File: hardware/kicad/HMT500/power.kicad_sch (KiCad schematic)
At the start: 22 parts, among them U1 TPS26600, U2 LMR36006, U3 TPS7A2033PDBVR

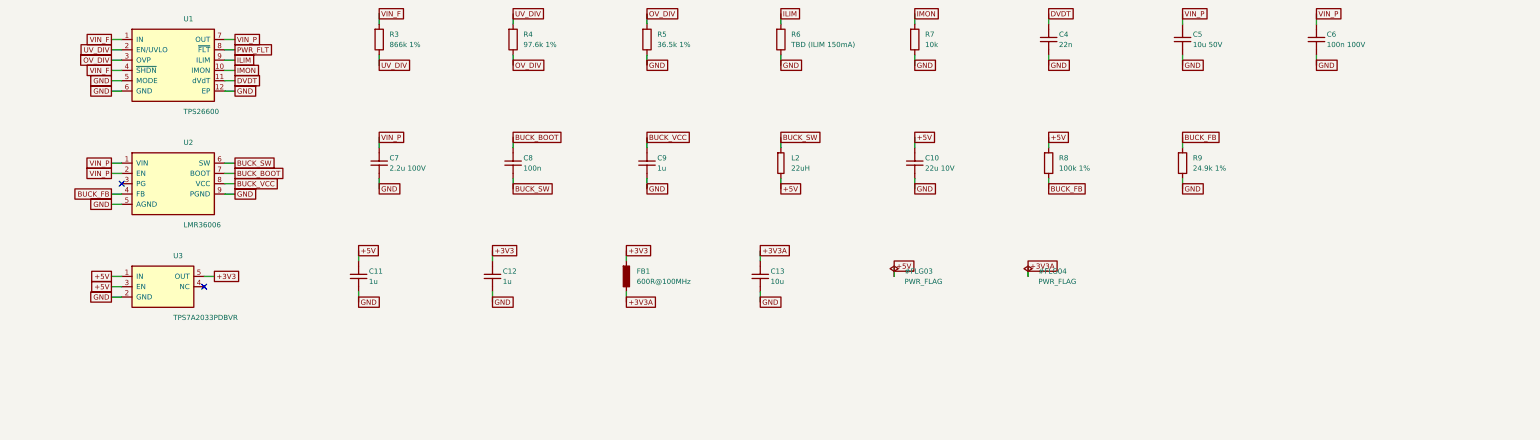
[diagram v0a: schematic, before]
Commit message: KiCad schematic v0.2: hand-laid-out, wired, readable sheets with power symbols and functional blocks
Replaces the label-only v0.1. Drawing rules are validated at generation and
the drawn netlist is checked against design intent (71 nets, 0 errors).

Co-Authored-By: Claude Opus 5.5 <noreply@anthropic.com>
Claude-Session: https://claude.ai/code/session_01JA2o8uJsqp9Vzsg4b665ev
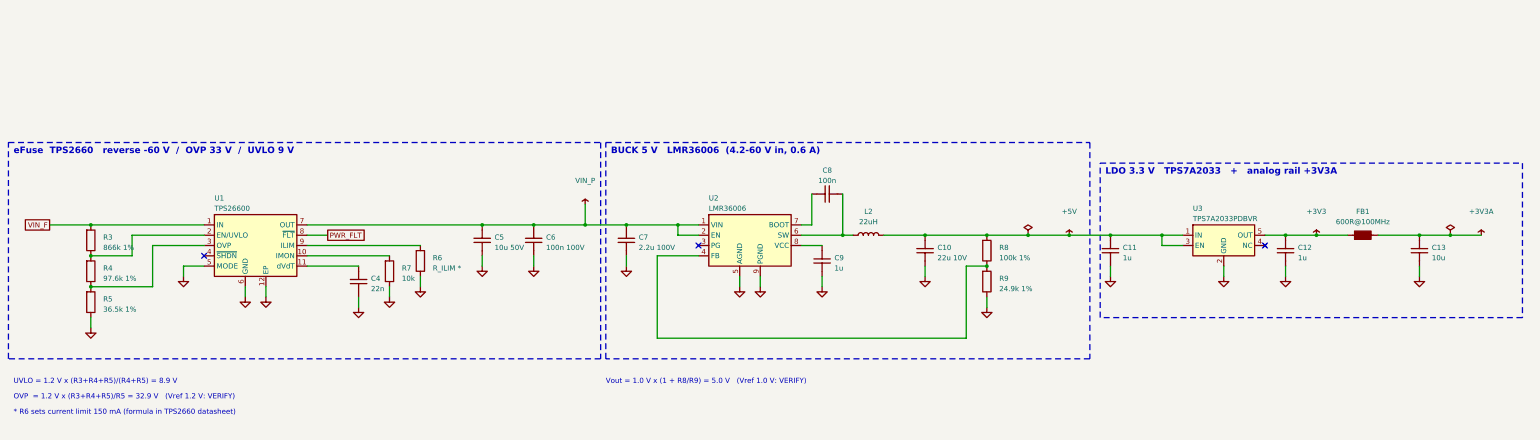
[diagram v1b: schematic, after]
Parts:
- C5, C7: footprint Capacitor_SMD:C_1206_3216Metric -> Capacitor_SMD:C_1210_3225Metric
- R6: value TBD (ILIM 150mA) -> R_ILIM *
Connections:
- net VIN_F: no longer U1.4 (~{SHDN})
- net BUCK_BOOT: no longer names the net of C8.1, U2.7 (BOOT)
- net BUCK_FB: no longer names the net of R8.2, R9.1, U2.4 (FB)
- net BUCK_SW: no longer names the net of C8.2, L2.1, U2.6 (SW)
- net BUCK_VCC: no longer names the net of C9.1, U2.8 (VCC)
- net DVDT: no longer names the net of C4.1, U1.11 (dVdT)
- net ILIM: no longer names the net of R6.1, U1.9 (ILIM)
- net IMON: no longer names the net of R7.1, U1.10 (IMON)
- net OV_DIV: no longer names the net of R4.2, R5.1, U1.3 (OVP)
- net UV_DIV: no longer names the net of R3.2, R4.1, U1.2 (EN/UVLO)
- no-connect marks 2 -> 3
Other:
- note added: "* R6 sets current limit 150 mA (formula in TPS2660 datasheet)"
- note added: "BUCK 5 V LMR36006 (4.2-60 V in, 0.6 A)"
- note added: "LDO 3.3 V TPS7A2033 + analog rail +3V3A"
- note added: "OVP = 1.2 V x (R3+R4+R5)/R5 = 32.9 V (Vref 1.2 V: VERIFY)"
- note added: "UVLO = 1.2 V x (R3+R4+R5)/(R4+R5) = 8.9 V"
- note added: "Vout = 1.0 V x (1 + R8/R9) = 5.0 V (Vref 1.0 V: VERIFY)"
- note added: "eFuse TPS2660 reverse -60 V / OVP 33 V / UVLO 9 V"
- title: HMT500 - eFuse, buck 5V, LDO 3.3V -> HMT500  Power
- moved on the sheet: C10, C11, C12, C13, C4, C5, C6, C7, C8, C9, R3, R4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

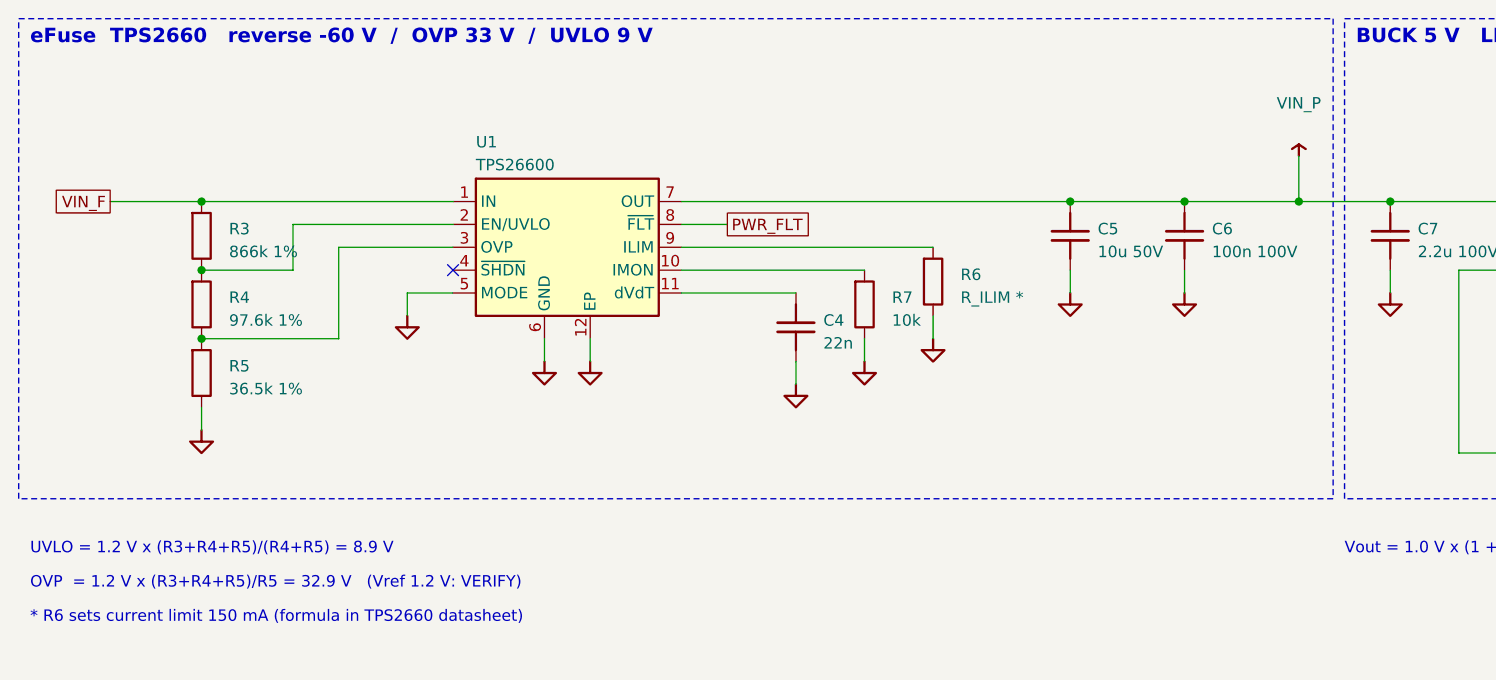
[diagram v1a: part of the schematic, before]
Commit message: Schematic v0.3, purchase parts list, studio product renders
- Schematic v0.3: TPS26600PWPR now uses the official KiCad pinout
  (HTSSOP-16: dual IN/OUT, UVLO, OVP, SHDN, MODE, RTN, EP). RTN is
  split onto its own net EF_RTN with a 0R link R22, flagged for
  datasheet confirmation, because tying RTN to GND disables the
  reverse-polarity protection. The ADS1220 pinout matches the official
  symbol. Netlist check passes: 70 nets, 0 errors. Rev bumped and cover
  notes updated.
- make_parts_list.py: purchase parts list (xlsx + csv) built from the
  KiCad BOM. It adds manufacturer, MPN, 1k price estimates and status,
  plus a per-category summary sheet with an FX input.
- render_studio.py: studio-style product renders (PBR stainless,
  image-based lighting, SSAO, contact shadow, laser marking, thread and
  connector pin detail). Six shots, including a cutaway.

Co-Authored-By: Claude Opus 5.5 <noreply@anthropic.com>
Claude-Session: https://claude.ai/code/session_01JA2o8uJsqp9Vzsg4b665ev
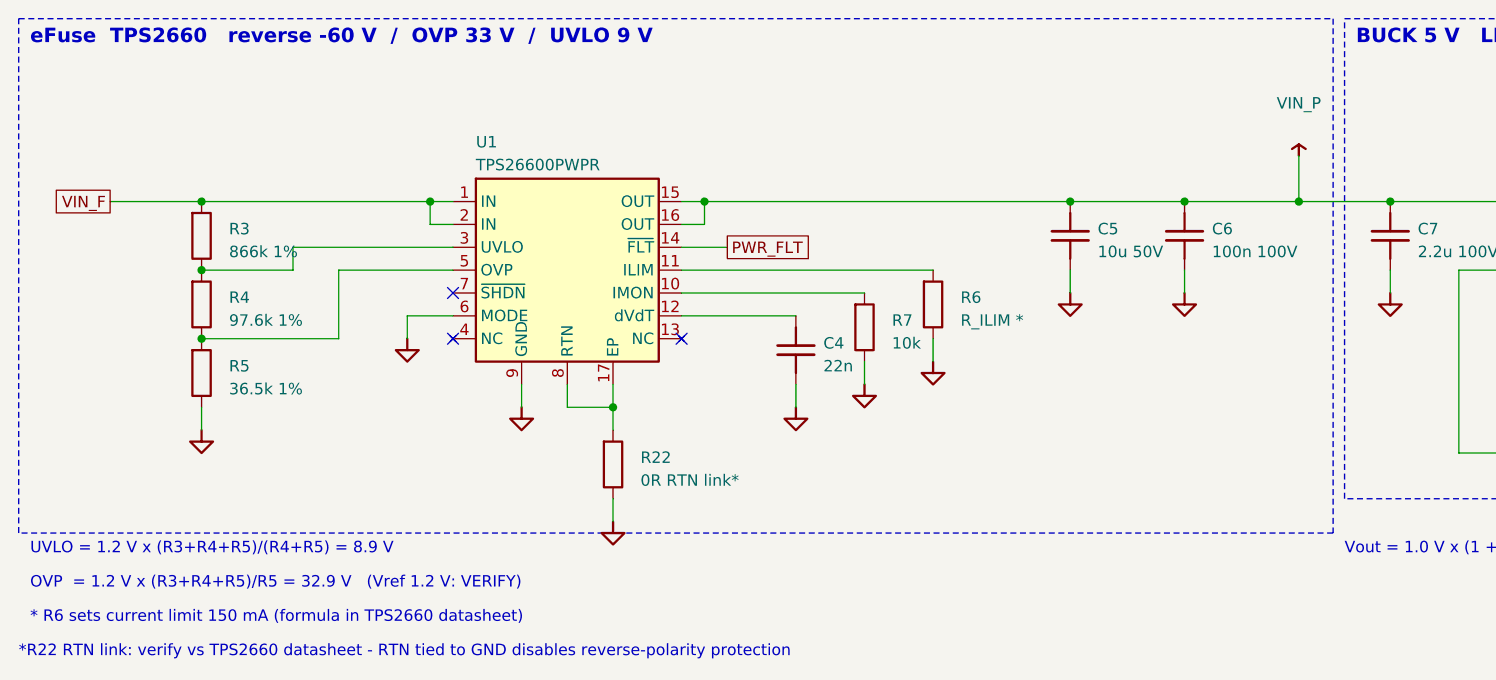
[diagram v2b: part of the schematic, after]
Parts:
- added R22: 0R RTN link*, Resistor_SMD:R_0603_1608Metric, symbol HMT500:R
- U1: value TPS26600 -> TPS26600PWPR; footprint TBD:HTSSOP-16_TPS2660 -> Package_SO:HTSSOP-16-1EP_4.4x5mm_P0.65mm_EP3.4x5mm_Mask2.66x2.46mm_ThermalVias
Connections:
- net GND: now also U1.9 (GND), R22.2; no longer U1.12 (EP), U1.5 (MODE)
- net PWR_FLT: now also U1.14 (~{FLT}); no longer U1.8 (~{FLT})
- net VIN_F: now also U1.2 (IN)
- net VIN_P: now also U1.15 (OUT), U1.16 (OUT); no longer U1.7 (OUT)
- net at R6.1: now also U1.11 (ILIM); no longer U1.9 (ILIM)
- net at R3.2, R4.1: now also U1.3 (UVLO); no longer U1.2 (EN/UVLO)
- net at R4.2, R5.1: now also U1.5 (OVP); no longer U1.3 (OVP)
- net at C4.1: now also U1.12 (dVdT); no longer U1.11 (dVdT)
- new net: R22.1, U1.17 (EP), U1.8 (RTN)
- no-connect marks 3 -> 5
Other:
- note added: "*R22 RTN link: verify vs TPS2660 datasheet - RTN tied to GND disables reverse-polarity protection"
- moved on the sheet: C4, R6, R7

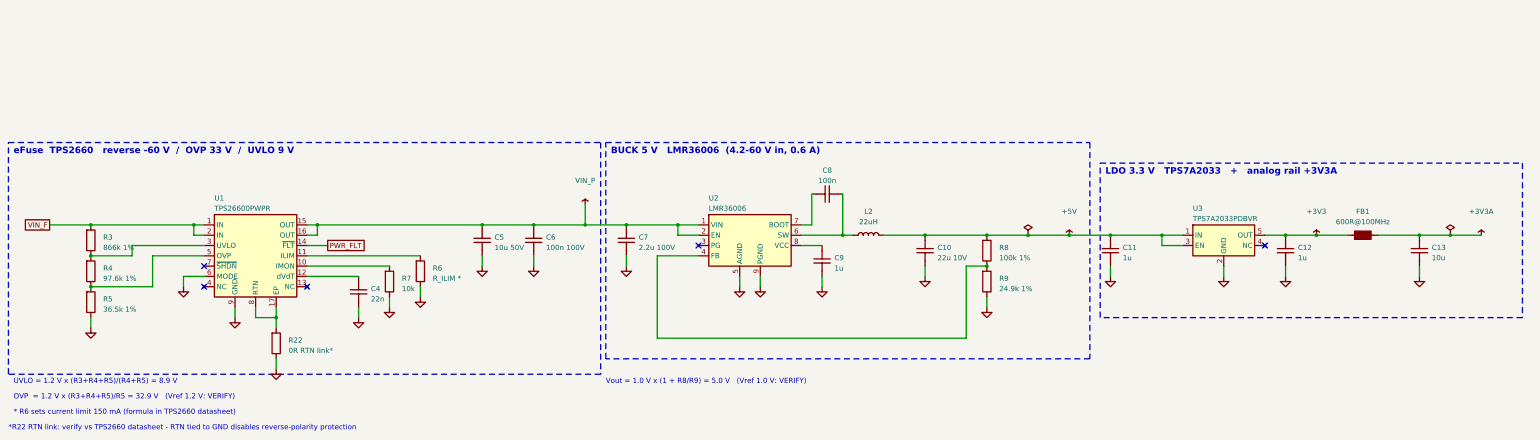
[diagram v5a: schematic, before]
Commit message: Schematic drawing rules: no overlapping text, Korean font, distinct net names
- Generator places reference/value text automatically, clear of symbol bodies,
  pins, wires, labels, notes and box edges; validation fails on any overlap
  (also note text vs wires/power names and bodies vs box edges)
- Fix 180-degree parts (LED) whose justification KiCad mirrors
- Styles: reference bold, value normal, power nets italic, signal nets boxed labels
- Korean box subtitles and legend in NanumGothic TrueType (stroke font has no Hangul)
- Nets renamed where they matched part or pin names: LED -> STAT_LED, EF_ILIM/IMON/DVDT
- J1 GH mounting pads removed from the symbol (PCB only); connector sheet re-spaced
- Schematic PDF export added; tests for net naming and Hangul font

Co-Authored-By: Claude Opus 5.5 <noreply@anthropic.com>
Claude-Session: https://claude.ai/code/session_01JA2o8uJsqp9Vzsg4b665ev
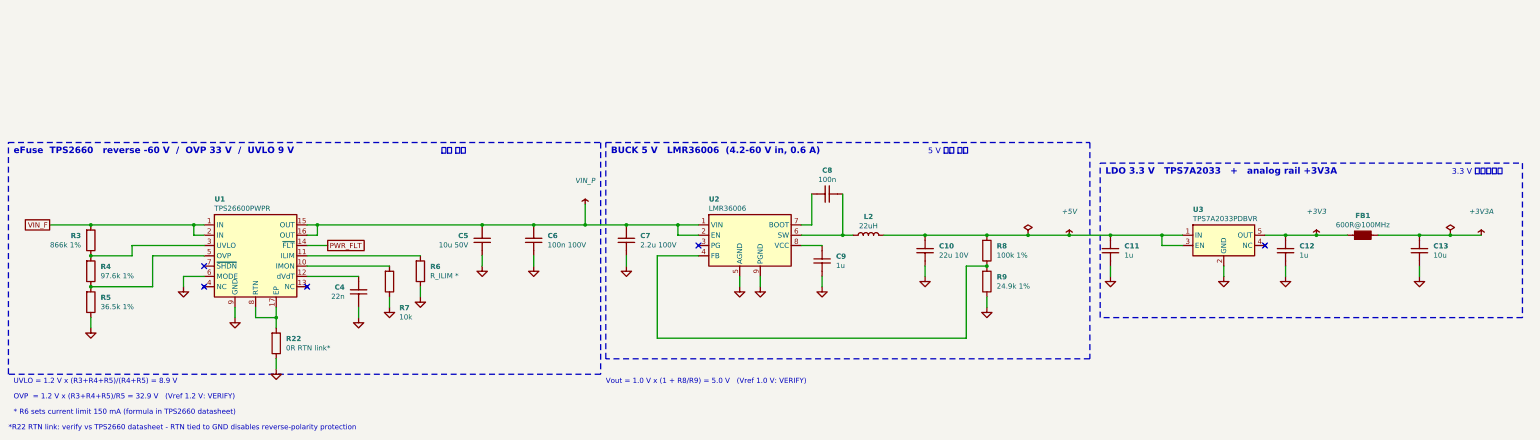
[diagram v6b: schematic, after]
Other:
- note added: "3.3 V 레귤레이터"
- note added: "5 V 강압 전원"
- note added: "전자 퓨즈"

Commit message: Schematic v0.6: parts cleanup (91 -> 75) and PCB temperature sensing
- Removed: fault pull-ups R11-R15 (MCU internal pull-ups), status LED D3/R16
  (not visible after potting), RS-485 R60/R61/D60/D61 (THVD2450 built-in
  protection), VREF+ filter FB2/C19 (MCU ADC only for diagnostics), C11/C2/C6
  (duplicated by adjacent capacitors); VREF+ tied to +3V3 with C20
- PCB temperature with no added parts: ADS1220 internal sensor at the measurement
  front, STM32G0 internal sensor mid-board; compensation plan in circuit-design 5B
- 63 nets, netlist check 0 errors; parts list regenerated; decision log #22/#23

Co-Authored-By: Claude Opus 5.5 <noreply@anthropic.com>
Claude-Session: https://claude.ai/code/session_01JA2o8uJsqp9Vzsg4b665ev
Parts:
- removed C11: 1u, Capacitor_SMD:C_0603_1608Metric, symbol HMT500:C
- removed C6: 100n 100V, Capacitor_SMD:C_0805_2012Metric, symbol HMT500:C

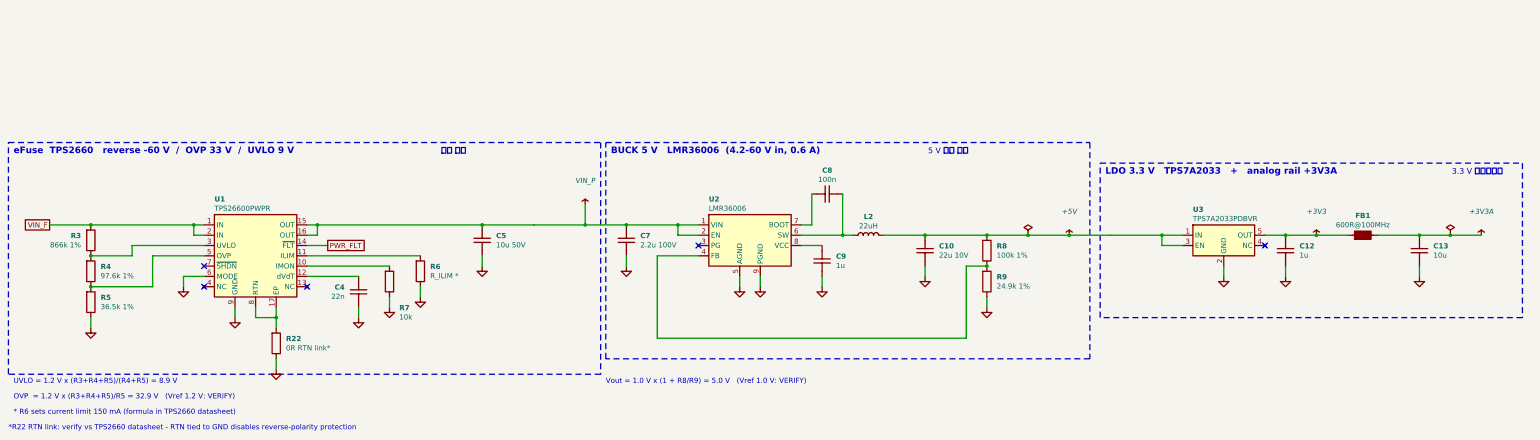
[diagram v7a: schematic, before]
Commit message: Schematic redraw: aligned parts, straight wires, fewer junctions
- Bends 54 -> 1, junctions 51 -> 31 (remaining are real 3-way nodes: divider taps,
  protection taps, tied pin pairs, power flags)
- Power pins get their own power symbols instead of rails with T-branches; signals
  between distant parts use labels; two-pin parts sit on the pin row they connect to
- Symbol pin order rearranged for straight runs (pin numbers unchanged): TPS2660,
  LMR36006 (BOOT on top), PCAP04 (Cref pins 3 rows apart, VDD18 on right), ADS1220
  (bottom pins 3 apart), DAC8760 (GND-tied pins on bottom), TPS26611 (FLT on bottom)
- New checks: pin names inside IC bodies must not overlap, boxes must not overlap;
  test limits bends per sheet and total junctions
- Netlist check 63 nets, 0 errors

Co-Authored-By: Claude Opus 5.5 <noreply@anthropic.com>
Claude-Session: https://claude.ai/code/session_01JA2o8uJsqp9Vzsg4b665ev
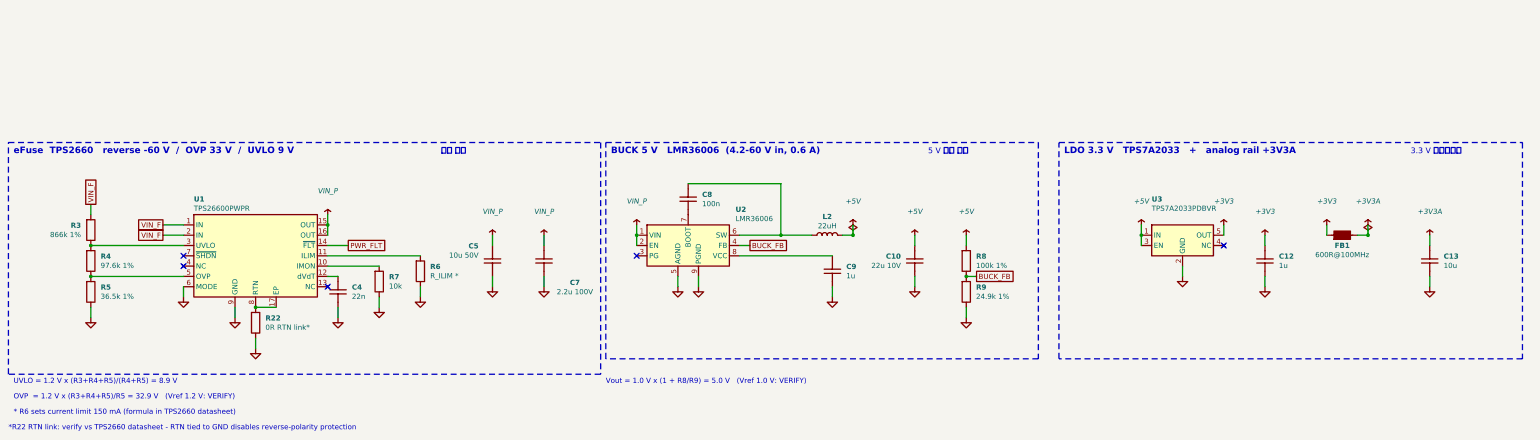
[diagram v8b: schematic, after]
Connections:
- net at L2.1, U2.6 (SW): now also C8.1; no longer C8.2
- net at U2.7 (BOOT): now also C8.2; no longer C8.1
- net BUCK_FB: now reaches R8.2, R9.1, U2.4 (FB)
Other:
- moved on the sheet: C10, C12, C13, C4, C5, C7, C8, C9, FB1, L2, R22, R3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
